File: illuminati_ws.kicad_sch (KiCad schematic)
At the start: 53 parts, among them IC1 ESP32-C3-WROOM-02-N4, J1 Conn_02x03_Odd_Even, J10 Conn_01x03, J11 Conn_01x03, J14 Conn_01x04, J2 Conn_01x03, J3 Conn_01x03, J4 Conn_01x03, J5 Conn_01x03, J7 Conn_01x03, J8 Conn_01x03, J9 Conn_01x03, SW1 SW_SPST, U2 74HC14, U3 74HC14, U4 74HC14, U6 AMS1117-3.3

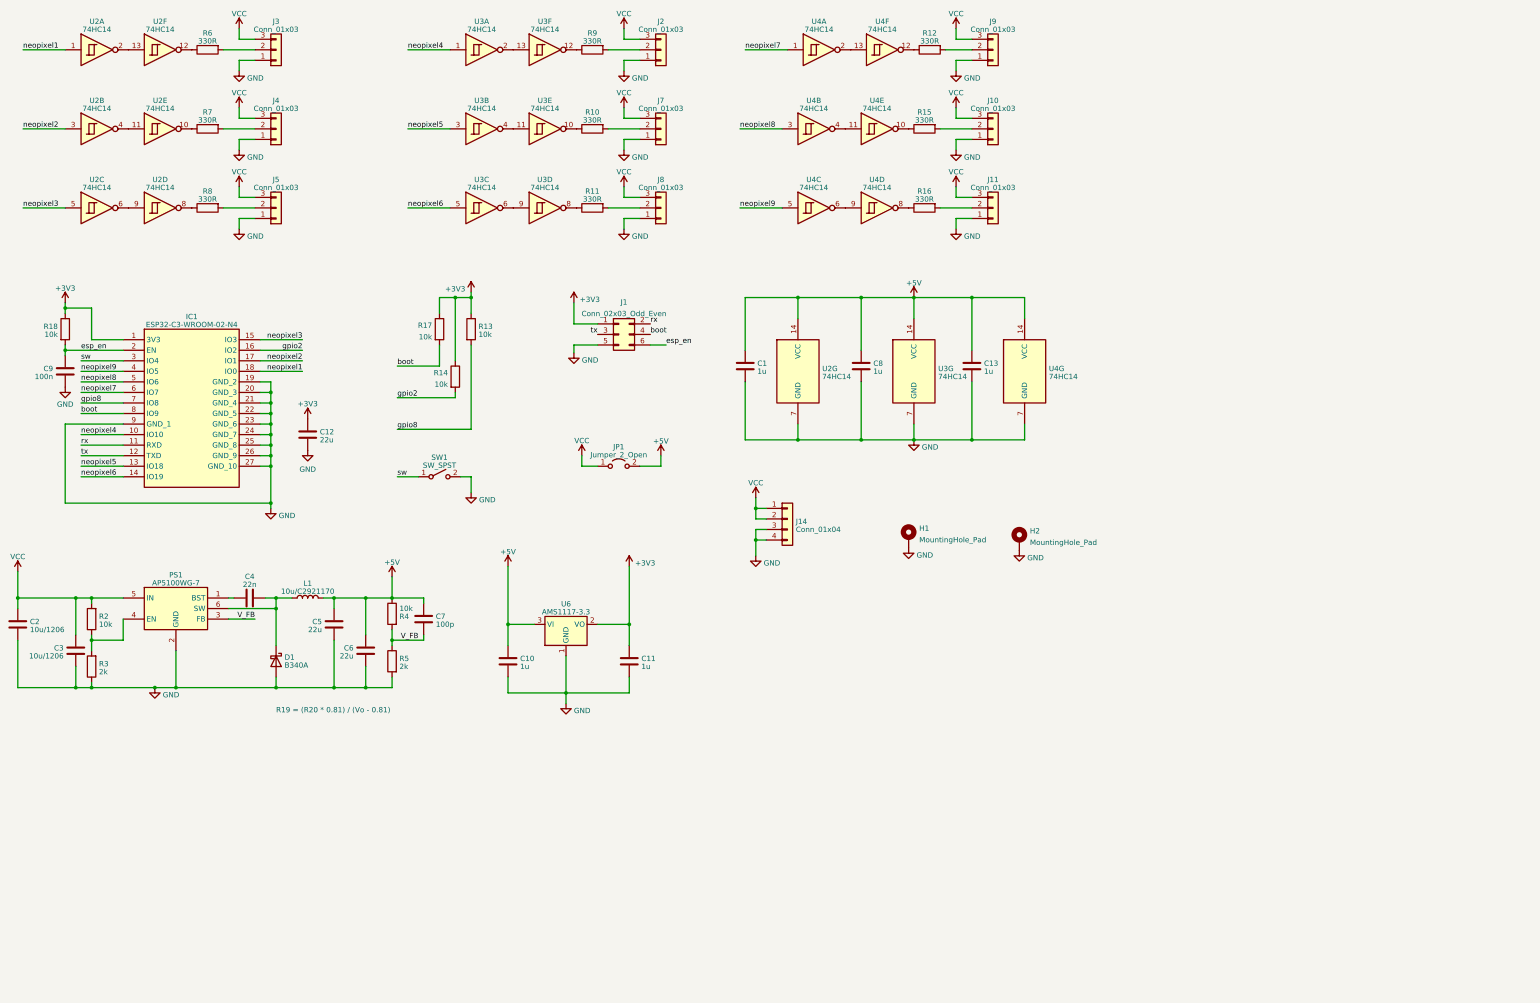
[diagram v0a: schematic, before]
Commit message: Board V2 swap esp32c3 for esp32
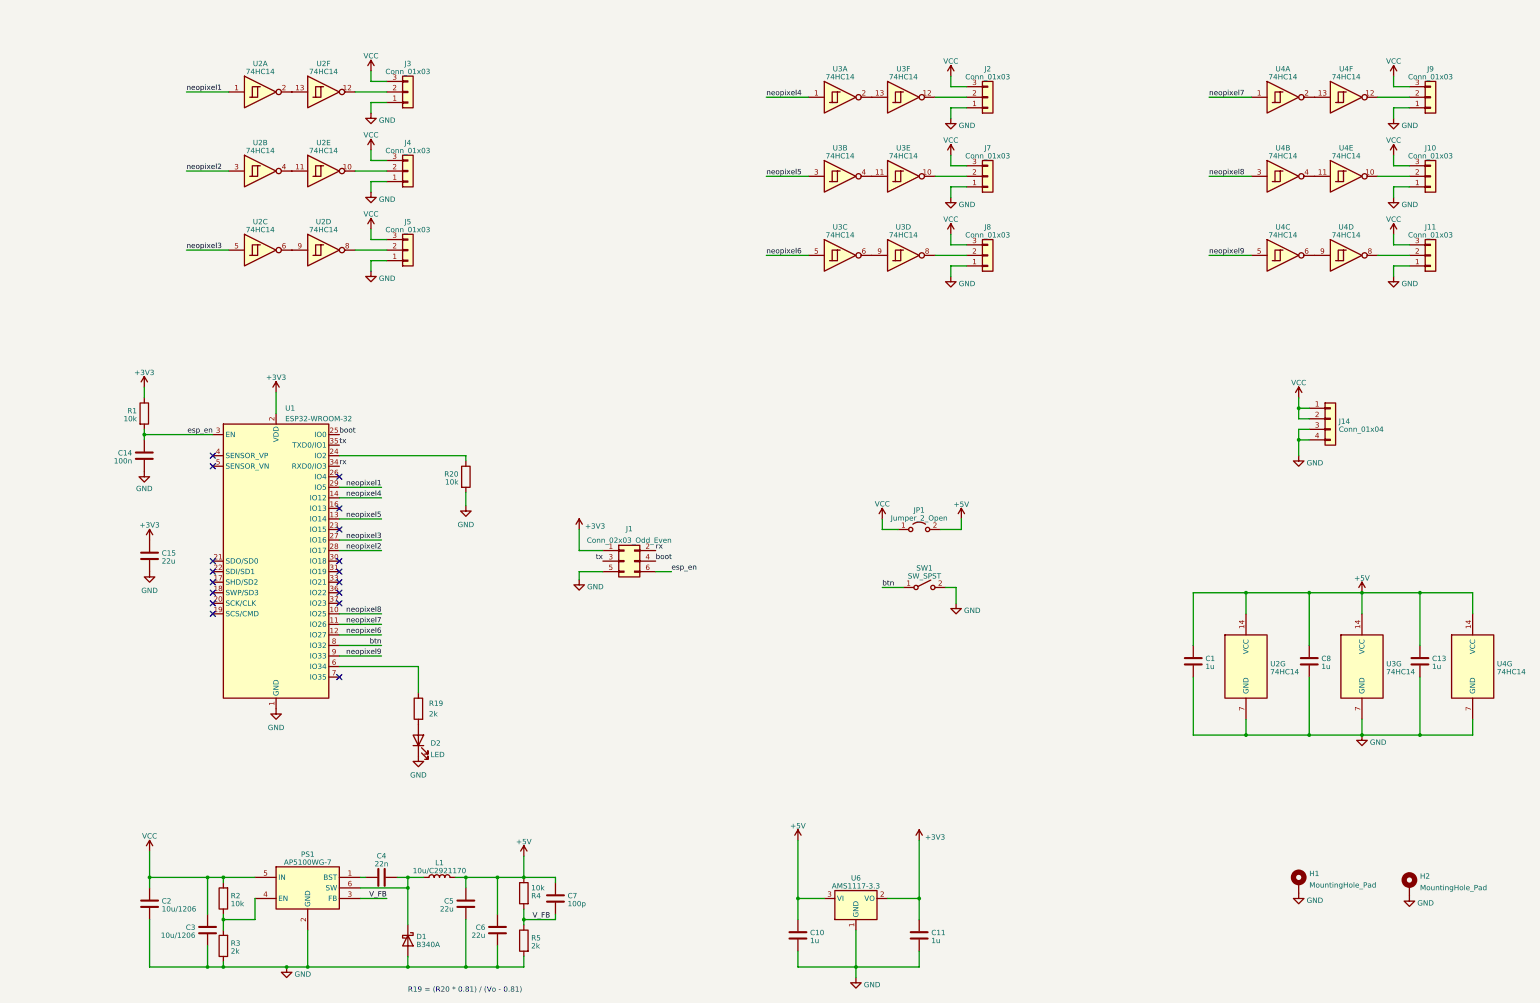
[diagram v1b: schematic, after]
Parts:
- removed C12: 22u, Capacitor_SMD:C_0805_2012Metric, symbol Device:C
- removed C9: 100n, Capacitor_SMD:C_0603_1608Metric, symbol Device:C
- removed IC1: ESP32-C3-WROOM-02-N4, SamacSys_Parts:ESP32C3WROOM02N4, symbol SamacSys_Parts:ESP32-C3-WROOM-02-N4
- removed R10, R11, R12, R15, R16, R6, R7, R8, R9: 330R, Resistor_SMD:R_0603_1608Metric, symbol Device:R
- removed R13, R14, R17, R18: 10k, Resistor_SMD:R_0603_1608Metric, symbol Device:R
- added C14: 100n, Capacitor_SMD:C_0603_1608Metric, symbol Device:C
- added C15: 22u, Capacitor_SMD:C_0805_2012Metric, symbol Device:C
- added D2: LED, LED_SMD:LED_0805_2012Metric, symbol Device:LED
- added R1, R20: 10k, Resistor_SMD:R_0603_1608Metric, symbol Device:R
- added R19: 2k, Resistor_SMD:R_0603_1608Metric, symbol Device:R
- added U1: ESP32-WROOM-32, RF_Module:ESP32-WROOM-32, symbol RF_Module:ESP32-WROOM-32
- C1, C10, C11, C13, C8: MPN (none) -> C28323
- C2, C3: MPN (none) -> C13585
- C4: MPN (none) -> C21122
- C5, C6: MPN (none) -> C45783
- C7: MPN (none) -> C1790
- D1: MPN (none) -> C3018525
- J10, J11, J2, J3, J4, J5, J7, J8, J9: MPN (none) -> C8401
- J14: MPN (none) -> C192769
- L1: MPN (none) -> C2921170
- PS1: MPN (none) -> C114647
- R2, R4: MPN (none) -> C25804
- R3, R5: MPN (none) -> C22975
- U2, U3, U4: MPN (none) -> C5967
- U6: MPN (none) -> C6186
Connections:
- net +3V3: now also C15.1, R1.1, U1.2 (VDD)
- net GND: now also C14.2, C15.2, D2.1 (K), R20.2, U1.1 (GND), U1.15 (GND), U1.38 (GND), U1.39 (GND)
- net boot: now also U1.25 (IO0)
- net esp_en: now also C14.1, R1.2, U1.3 (EN)
- net neopixel1: now also U1.29 (IO5)
- net neopixel2: now also U1.28 (IO17)
- net neopixel3: now also U1.27 (IO16)
- net neopixel4: now also U1.14 (IO12)
- net neopixel5: now also U1.13 (IO14)
- net neopixel6: now also U1.12 (IO27)
- net neopixel7: now also U1.11 (IO26)
- net neopixel8: now also U1.10 (IO25)
- net neopixel9: now also U1.9 (IO33)
- net rx: now also U1.34 (RXD0/IO3)
- net tx: now also U1.35 (TXD0/IO1)
- net at J2.2 (Pin_2): now also U3.12
- net at U2.10: now also J4.2 (Pin_2)
- net at U4.12: now also J9.2 (Pin_2)
- net at U3.8: now also J8.2 (Pin_2)
- net at U3.10: now also J7.2 (Pin_2)
- net at U4.10: now also J10.2 (Pin_2)
- net at U2.12: now also J3.2 (Pin_2)
- net at U4.8: now also J11.2 (Pin_2)
- net at U2.8: now also J5.2 (Pin_2)
- net sw renamed btn
- net btn: now also U1.8 (IO32)
- new net: R19.1, U1.6 (IO34)
- new net: D2.2 (A), R19.2
- new net: R20.1, U1.24 (IO2)
- no-connect marks 0 -> 17
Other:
- moved on the sheet: C1, C10, C11, C13, C2, C3, C4, C5, C6, C7, C8, D1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
